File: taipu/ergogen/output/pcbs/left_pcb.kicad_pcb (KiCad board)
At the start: 2 copper layers, 145 x 92.4 mm, 1 part

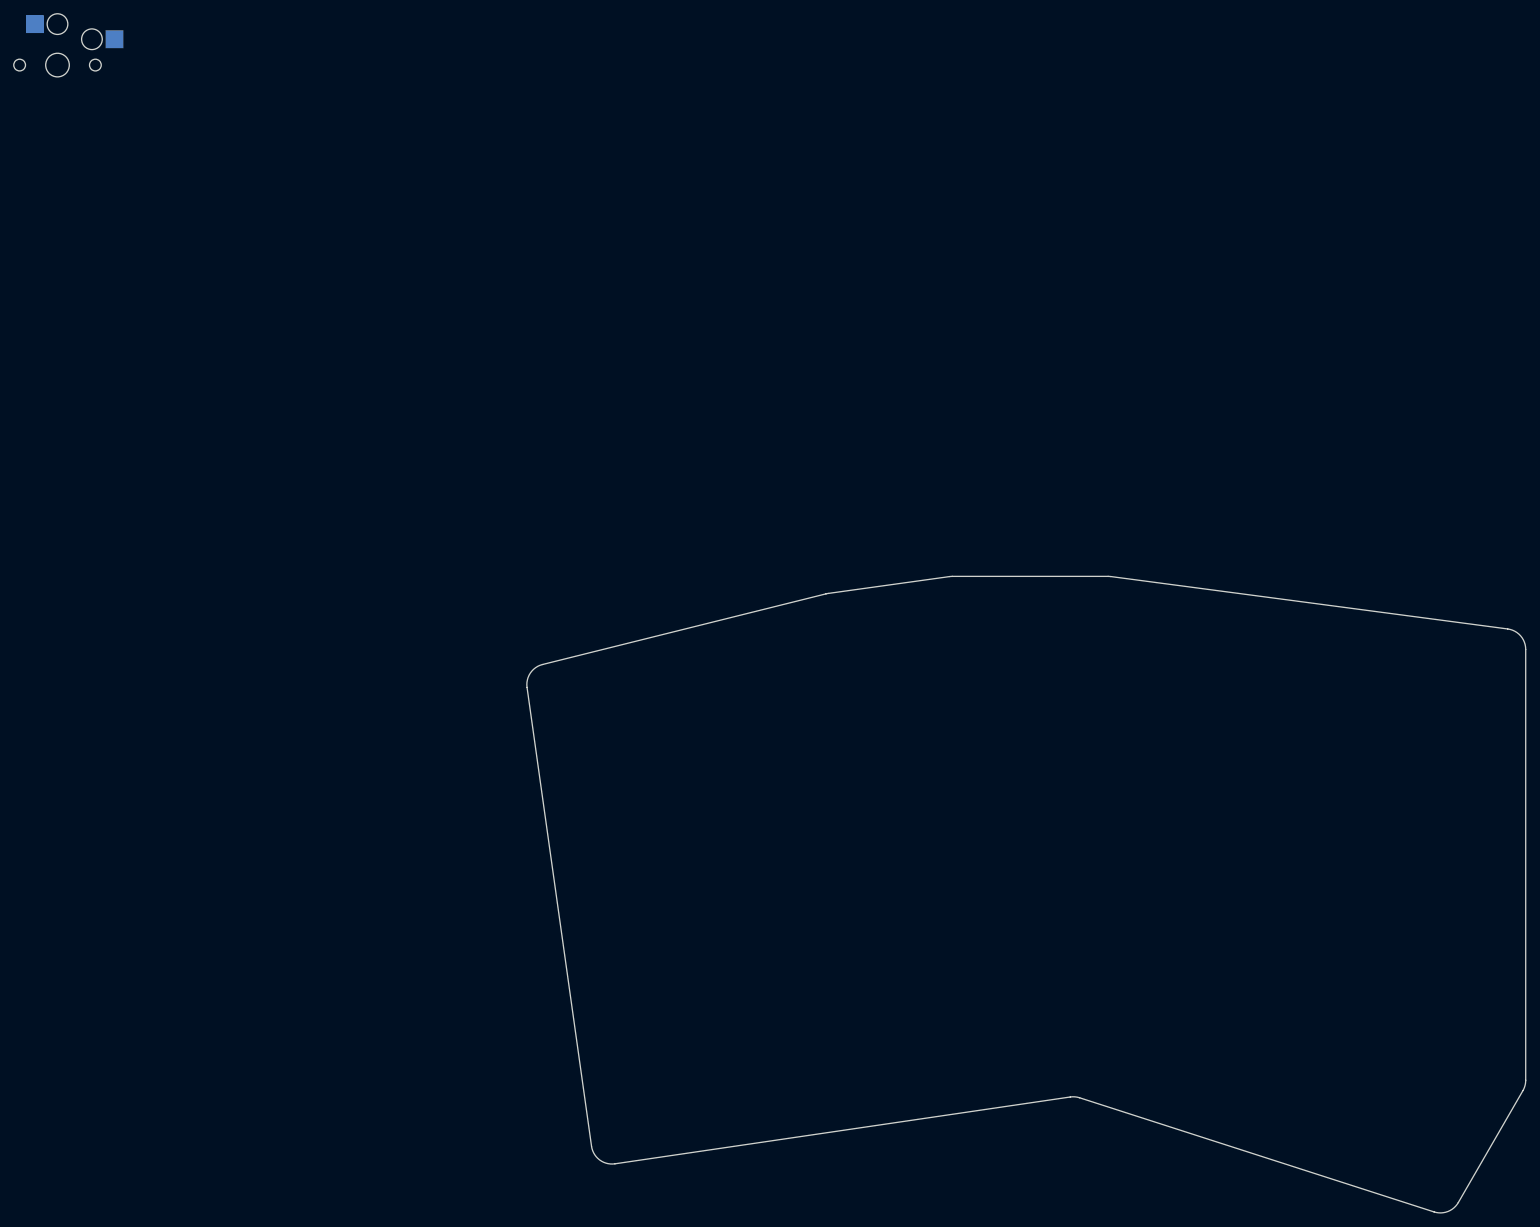
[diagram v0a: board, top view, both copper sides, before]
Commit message: mounting holes and net
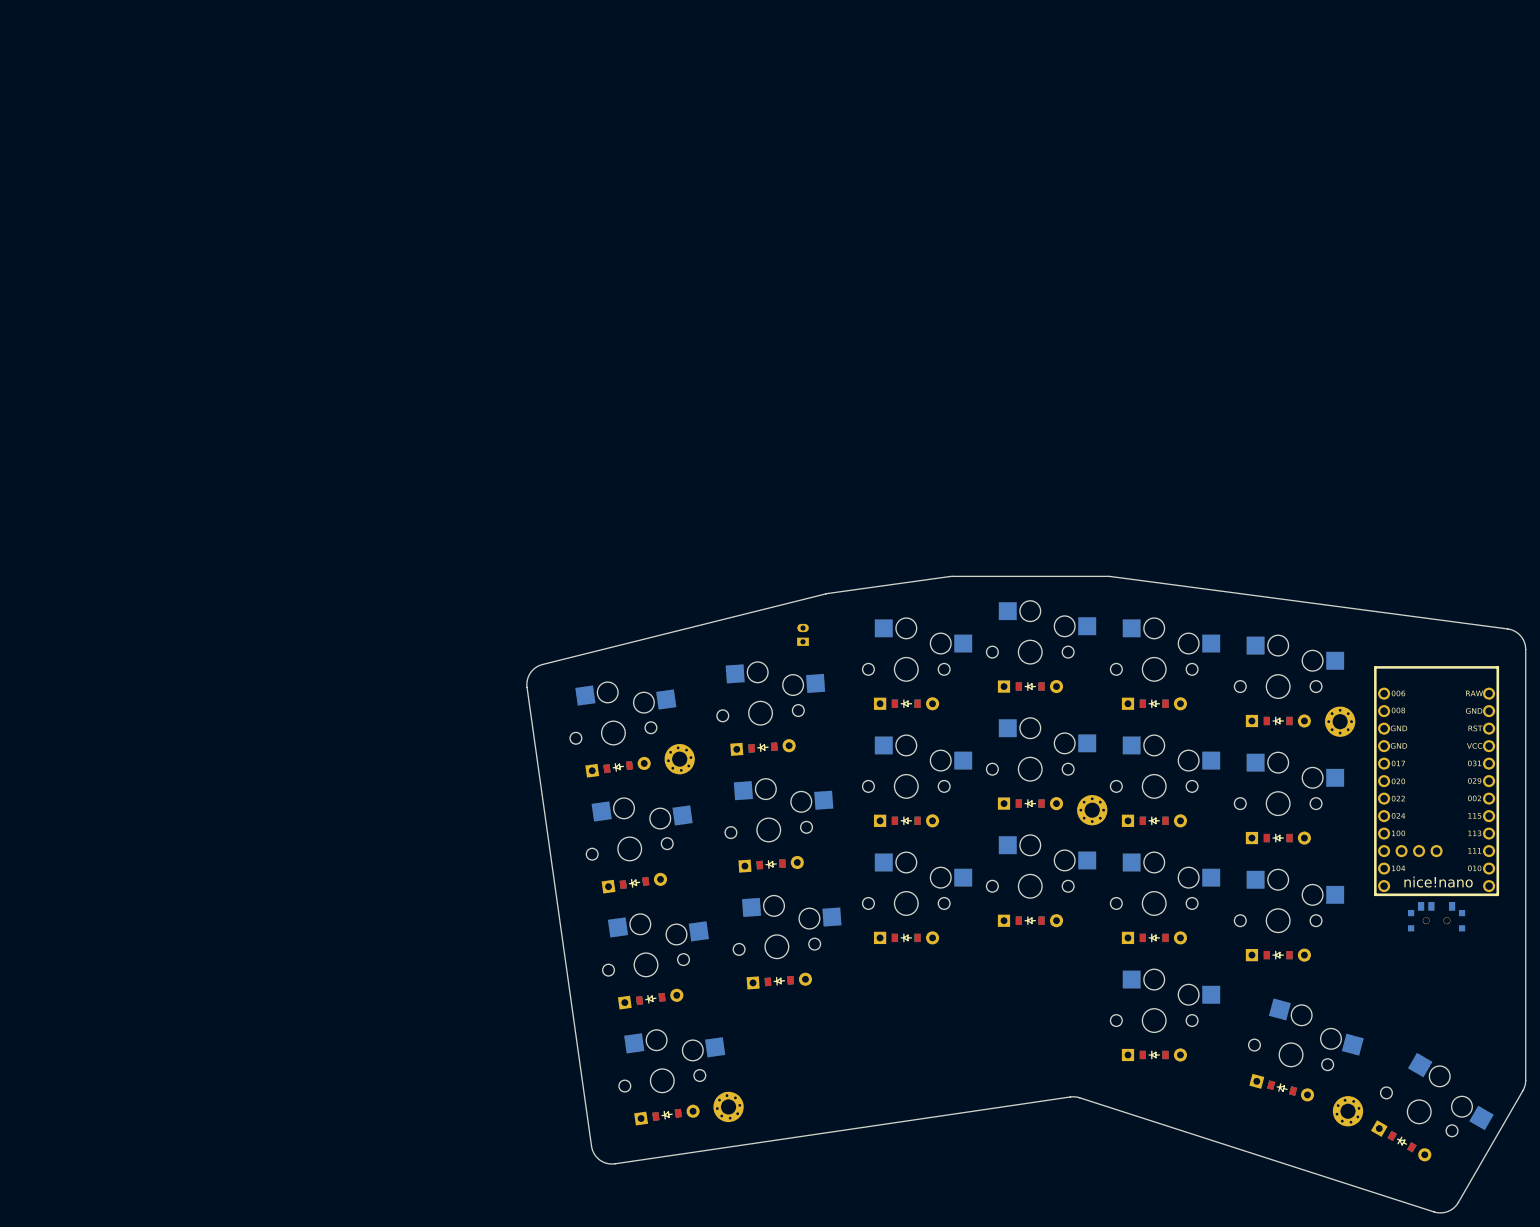
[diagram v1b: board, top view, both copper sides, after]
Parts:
- added D1: , ComboDiode, F.Cu at (88.5, 152.4)
- added D10: , ComboDiode, F.Cu at (123.3, 92.7)
- added D11: , ComboDiode, F.Cu at (141.3, 124.2)
- added D12: , ComboDiode, F.Cu at (141.3, 107.2)
- added D13: , ComboDiode, F.Cu at (141.3, 90.2)
- added D14: , ComboDiode, F.Cu at (159.3, 143.7)
- added D15: , ComboDiode, F.Cu at (159.3, 126.7)
- added D16: , ComboDiode, F.Cu at (159.3, 109.7)
- added D17: , ComboDiode, F.Cu at (159.3, 92.7)
- added D18: , ComboDiode, F.Cu at (177.3, 129.2)
- added D19: , ComboDiode, F.Cu at (177.3, 112.2)
- added D2: , ComboDiode, F.Cu at (86.2, 135.6)
- added D20: , ComboDiode, F.Cu at (177.3, 95.2)
- added D21: , ComboDiode, F.Cu at (177.8, 148.6)
- added D22: , ComboDiode, F.Cu at (195.2, 156.3)
- added D3: , ComboDiode, F.Cu at (83.8, 118.8)
- added D4: , ComboDiode, F.Cu at (81.4, 101.9)
- added D5: , ComboDiode, F.Cu at (104.8, 133.0)
- added D6: , ComboDiode, F.Cu at (103.6, 116.1)
- added D7: , ComboDiode, F.Cu at (102.4, 99.1)
- added D8: , ComboDiode, F.Cu at (123.3, 126.7)
- added D9: , ComboDiode, F.Cu at (123.3, 109.7)
- added JST1: , JST_PH_S2B-PH-K_02x2.00mm_Angled, F.Cu at (108.3, 82.7)
- added MCU1: nice_nano, nice_nano, F.Cu at (200.3, 105.2)
- added S10: , PG1350, F.Cu at (123.3, 87.7)
- added S11: , PG1350, F.Cu at (141.3, 119.2)
- added S12: , PG1350, F.Cu at (141.3, 102.2)
- added S13: , PG1350, F.Cu at (141.3, 85.2)
- added S14: , PG1350, F.Cu at (159.3, 138.7)
- added S15: , PG1350, F.Cu at (159.3, 121.7)
- added S16: , PG1350, F.Cu at (159.3, 104.7)
- added S17: , PG1350, F.Cu at (159.3, 87.7)
- added S18: , PG1350, F.Cu at (177.3, 124.2)
- added S19: , PG1350, F.Cu at (177.3, 107.2)
- added S2: , PG1350, F.Cu at (85.5, 130.7)
- added S20: , PG1350, F.Cu at (177.3, 90.2)
- added S21: , PG1350, F.Cu at (179.1, 143.7)
- added S22: , PG1350, F.Cu at (197.7, 152.0)
- added S3: , PG1350, F.Cu at (83.1, 113.8)
- added S4: , PG1350, F.Cu at (80.7, 97.0)
- added S5: , PG1350, F.Cu at (104.5, 128.0)
- added S6: , PG1350, F.Cu at (103.3, 111.1)
- added S7: , PG1350, F.Cu at (102.1, 94.1)
- added S8: , PG1350, F.Cu at (123.3, 121.7)
- added S9: , PG1350, F.Cu at (123.3, 104.7)
- added T1: , E73:SPDT_C128955, F.Cu at (200.3, 124.2)
- added _1: , MountingHole_2.2mm_M2_Pad_Via, F.Cu at (90.3, 100.8)
- added _2: , MountingHole_2.2mm_M2_Pad_Via, F.Cu at (186.3, 95.3)
- added _3: , MountingHole_2.2mm_M2_Pad_Via, F.Cu at (150.3, 108.2)
- added _4: , MountingHole_2.2mm_M2_Pad_Via, F.Cu at (97.4, 151.3)
- added _5: , MountingHole_2.2mm_M2_Pad_Via, F.Cu at (187.4, 151.9)
- moved S1 171.7 mm to (87.8, 147.5), turned to 8 degrees
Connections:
- S1 pad 1: (no net) -> P020
- S1 pad 2: (no net) -> outer_mod

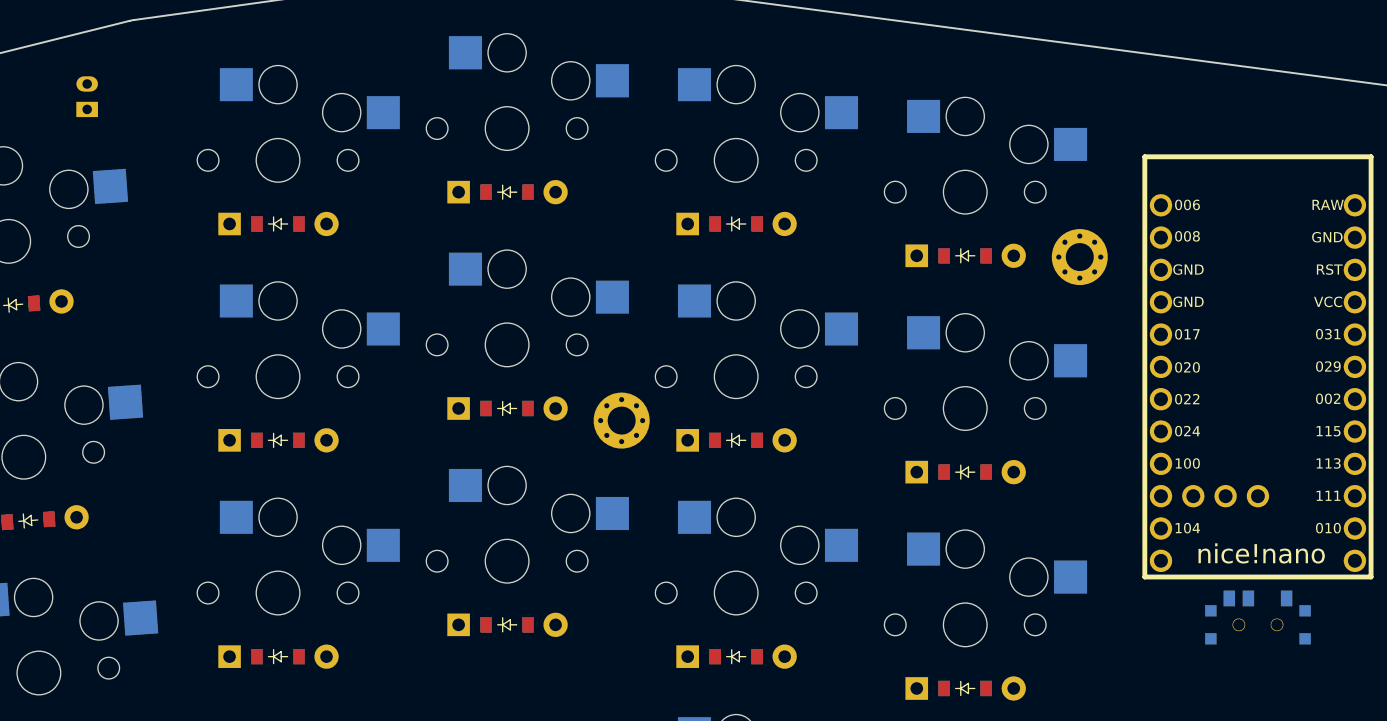
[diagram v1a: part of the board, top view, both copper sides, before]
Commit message: better batery placement
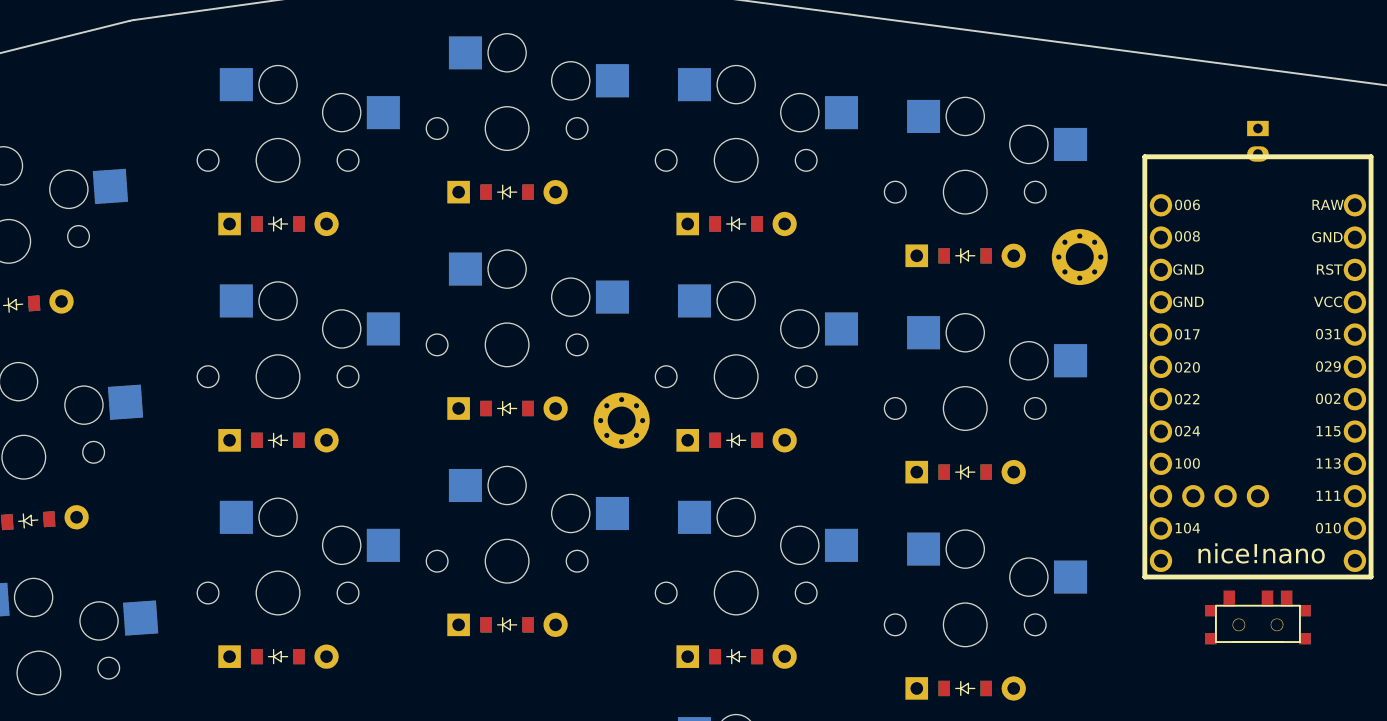
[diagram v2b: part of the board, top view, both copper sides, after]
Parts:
- moved JST1 92.1 mm to (200.3, 86.2), turned to -90 degrees
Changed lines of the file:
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@@
         (descr "JST PH series connector, S2B-PH-K, side entry type, through hole, Datasheet: http://www.jst-mfg.com/product/pdf/eng/ePH.pdf")
         (tags "connector jst ph")
-        (at 108.25702100000001 82.74633159999999 90)
+        (at 200.257021 86.24633159999999 -90)
         (fp_text reference "JST1" (at 0 0) (layer F.SilkS) hide (effects (font (size 1.27 1.27) (thickness 0.15))))
         (fp_text value "" (at 0 0) (layer F.SilkS) hide (effects (font (size 1.27 1.27) (thickness 0.15))))
@@
         (fp_line (start -1 1.5) (end -1 2.0) (layer B.SilkS) (width 0.15))
         (fp_line (start -1.25 1.75) (end -0.75 1.75) (layer B.SilkS) (width 0.15))
-        (pad 1 thru_hole rect (at -1 0 90) (size 1.2 1.7) (drill 0.75) (layers *.Cu *.Mask) (net 48 "pos"))
-        (pad 2 thru_hole oval (at 1 0 90) (size 1.2 1.7) (drill 0.75) (layers *.Cu *.Mask) (net 34 "GND"))
+        (pad 1 thru_hole rect (at -1 0 -90) (size 1.2 1.7) (drill 0.75) (layers *.Cu *.Mask) (net 48 "pos"))
+        (pad 2 thru_hole oval (at 1 0 -90) (size 1.2 1.7) (drill 0.75) (layers *.Cu *.Mask) (net 34 "GND"))
     )
         (module E73:SPDT_C128955 (layer F.Cu)
@@
             (fp_text reference "T1" (at 0 0) (layer F.SilkS) hide (effects (font (size 1.27 1.27) (thickness 0.15))))
             (fp_text value "" (at 0 0) (layer F.SilkS) hide (effects (font (size 1.27 1.27) (thickness 0.15))))
-            (fp_line (start 1.95 -1.35) (end -1.95 -1.35) (layer B.SilkS) (width 0.15))
-            (fp_line (start 0 -1.35) (end -3.3 -1.35) (layer B.SilkS) (width 0.15))
-            (fp_line (start -3.3 -1.35) (end -3.3 1.5) (layer B.SilkS) (width 0.15))
-            (fp_line (start -3.3 1.5) (end 3.3 1.5) (layer B.SilkS) (width 0.15))
-            (fp_line (start 3.3 1.5) (end 3.3 -1.35) (layer B.SilkS) (width 0.15))
-            (fp_line (start 0 -1.35) (end 3.3 -1.35) (layer B.SilkS) (width 0.15))
+            (fp_line (start 1.95 -1.35) (end -1.95 -1.35) (layer F.SilkS) (width 0.15))
+            (fp_line (start 0 -1.35) (end -3.3 -1.35) (layer F.SilkS) (width 0.15))
+            (fp_line (start -3.3 -1.35) (end -3.3 1.5) (layer F.SilkS) (width 0.15))
+            (fp_line (start -3.3 1.5) (end 3.3 1.5) (layer F.SilkS) (width 0.15))
+            (fp_line (start 3.3 1.5) (end 3.3 -1.35) (layer F.SilkS) (width 0.15))
+            (fp_line (start 0 -1.35) (end 3.3 -1.35) (layer F.SilkS) (width 0.15))
             (fp_line (start -1.95 -3.85) (end 1.95 -3.85) (layer Dwgs.User) (width 0.15))
             (fp_line (start 1.95 -3.85) (end 1.95 -1.35) (layer Dwgs.User) (width 0.15))
@@
             (pad "" np_thru_hole circle (at 1.5 0) (size 1 1) (drill 0.9) (layers *.Cu *.Mask))
             (pad "" np_thru_hole circle (at -1.5 0) (size 1 1) (drill 0.9) (layers *.Cu *.Mask))
-            (pad 1 smd rect (at -2.25 2.075 -180) (size 0.9 1.25) (layers B.Cu B.Paste B.Mask) (net 48 "pos"))
-            (pad 2 smd rect (at 0.75 2.075 -180) (size 0.9 1.25) (layers B.Cu B.Paste B.Mask) (net 33 "RAW"))
-            (pad 3 smd rect (at 2.25 2.075 -180) (size 0.9 1.25) (layers B.Cu B.Paste B.Mask))
-            (pad "" smd rect (at 3.7 -1.1 -180) (size 0.9 0.9) (layers B.Cu B.Paste B.Mask))
-            (pad "" smd rect (at 3.7 1.1 -180) (size 0.9 0.9) (layers B.Cu B.Paste B.Mask))
-            (pad "" smd rect (at -3.7 1.1 -180) (size 0.9 0.9) (layers B.Cu B.Paste B.Mask))
-            (pad "" smd rect (at -3.7 -1.1 -180) (size 0.9 0.9) (layers B.Cu B.Paste B.Mask))
+            (pad 1 smd rect (at 2.25 2.075 -180) (size 0.9 1.25) (layers F.Cu F.Paste F.Mask) (net 48 "pos"))
+            (pad 2 smd rect (at -0.75 2.075 -180) (size 0.9 1.25) (layers F.Cu F.Paste F.Mask) (net 33 "RAW"))
+            (pad 3 smd rect (at -2.25 2.075 -180) (size 0.9 1.25) (layers F.Cu F.Paste F.Mask))
+            (pad "" smd rect (at 3.7 -1.1 -180) (size 0.9 0.9) (layers F.Cu F.Paste F.Mask))
+            (pad "" smd rect (at 3.7 1.1 -180) (size 0.9 0.9) (layers F.Cu F.Paste F.Mask))
+            (pad "" smd rect (at -3.7 1.1 -180) (size 0.9 0.9) (layers F.Cu F.Paste F.Mask))
+            (pad "" smd rect (at -3.7 -1.1 -180) (size 0.9 0.9) (layers F.Cu F.Paste F.Mask))
         )
     (module "MountingHole_2.2mm_M2_Pad_Via" (version 20210722) (generator pcbnew) (layer "F.Cu")
